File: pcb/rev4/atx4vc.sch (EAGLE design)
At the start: 48 parts, among them IC1 MY_7905DT, J2 ATX24RH

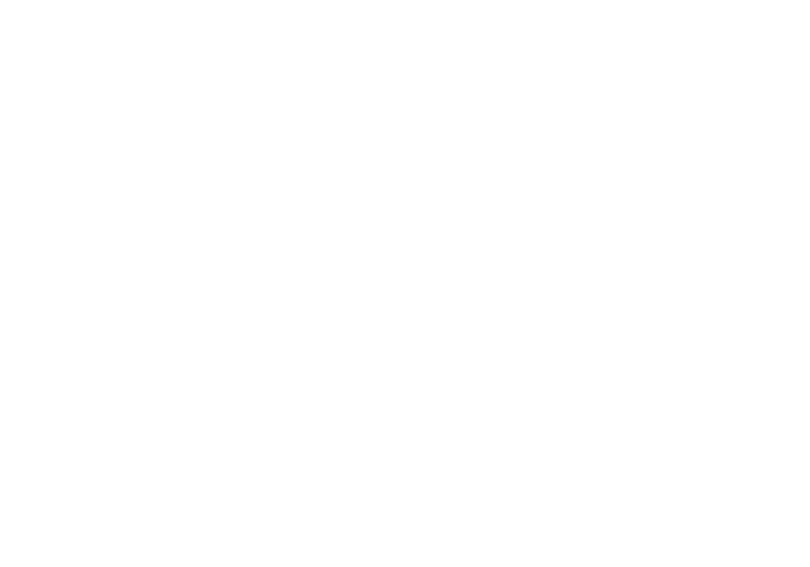
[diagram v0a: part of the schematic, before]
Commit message: trying out power ic
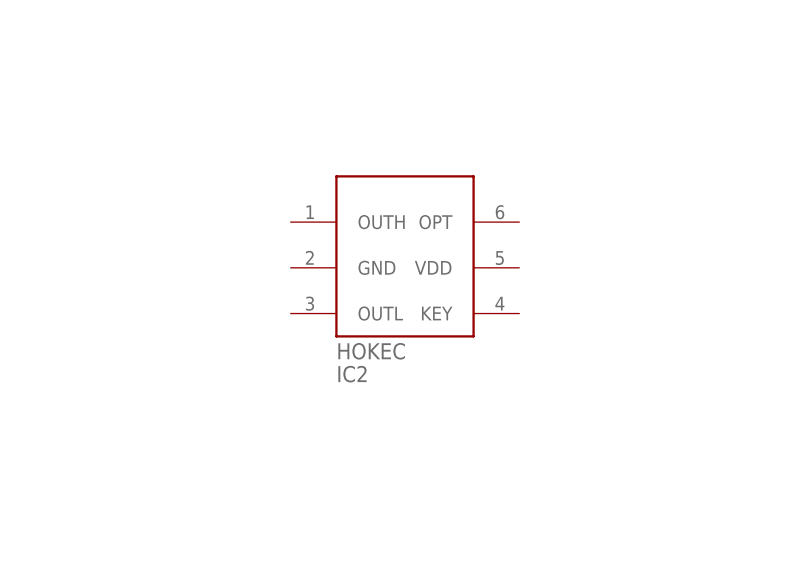
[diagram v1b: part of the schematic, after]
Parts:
- added IC2: MAX486X/SOT, pmm:MAX486X/SOT
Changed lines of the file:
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@@
 <layer number="154" name="FabDoc2" color="7" fill="1" visible="yes" active="yes"/>
 <layer number="155" name="FabDoc3" color="7" fill="1" visible="yes" active="yes"/>
+<layer number="156" name="gesam-Maß" color="7" fill="1" visible="yes" active="yes"/>
+<layer number="157" name="FaceMchng" color="7" fill="1" visible="yes" active="yes"/>
+<layer number="158" name="FaceMMeas" color="7" fill="1" visible="yes" active="yes"/>
+<layer number="159" name="Geh-Bear2" color="7" fill="1" visible="yes" active="yes"/>
+<layer number="160" name="O_Dim" color="7" fill="1" visible="yes" active="yes"/>
+<layer number="161" name="tomplace2" color="7" fill="1" visible="yes" active="yes"/>
 <layer number="166" name="AntennaArea" color="7" fill="1" visible="yes" active="yes"/>
 <layer number="168" name="4mmHeightArea" color="7" fill="1" visible="yes" active="yes"/>
@@
 <layer number="250" name="Descript" color="3" fill="1" visible="no" active="no"/>
 <layer number="251" name="SMDround" color="12" fill="11" visible="no" active="no"/>
+<layer number="252" name="BR-BS" color="7" fill="1" visible="yes" active="yes"/>
 <layer number="253" name="Extra" color="7" fill="1" visible="yes" active="yes"/>
 <layer number="254" name="cooling" color="7" fill="1" visible="yes" active="yes"/>
@@
 <part name="TP2" library="testpad" library_urn="urn:adsk.eagle:library:385" deviceset="TP" device="TP12R" package3d_urn="urn:adsk.eagle:package:27963/1"/>
 <part name="JP1" library="appleii" deviceset="4PIN_FAN" device=""/>
+<part name="IC2" library="pmm" deviceset="MAX486X" device="/SOT"/>
 </parts>
 <sheets>
@@
 </instance>
 <instance part="JP1" gate="A" x="223.52" y="-93.98" smashed="yes" rot="R180"/>
+<instance part="IC2" gate="G$1" x="121.92" y="81.28" smashed="yes">
+<attribute name="NAME" x="114.3" y="66.04" size="1.778" layer="95" font="vector"/>
+</instance>
 </instances>
 <busses>

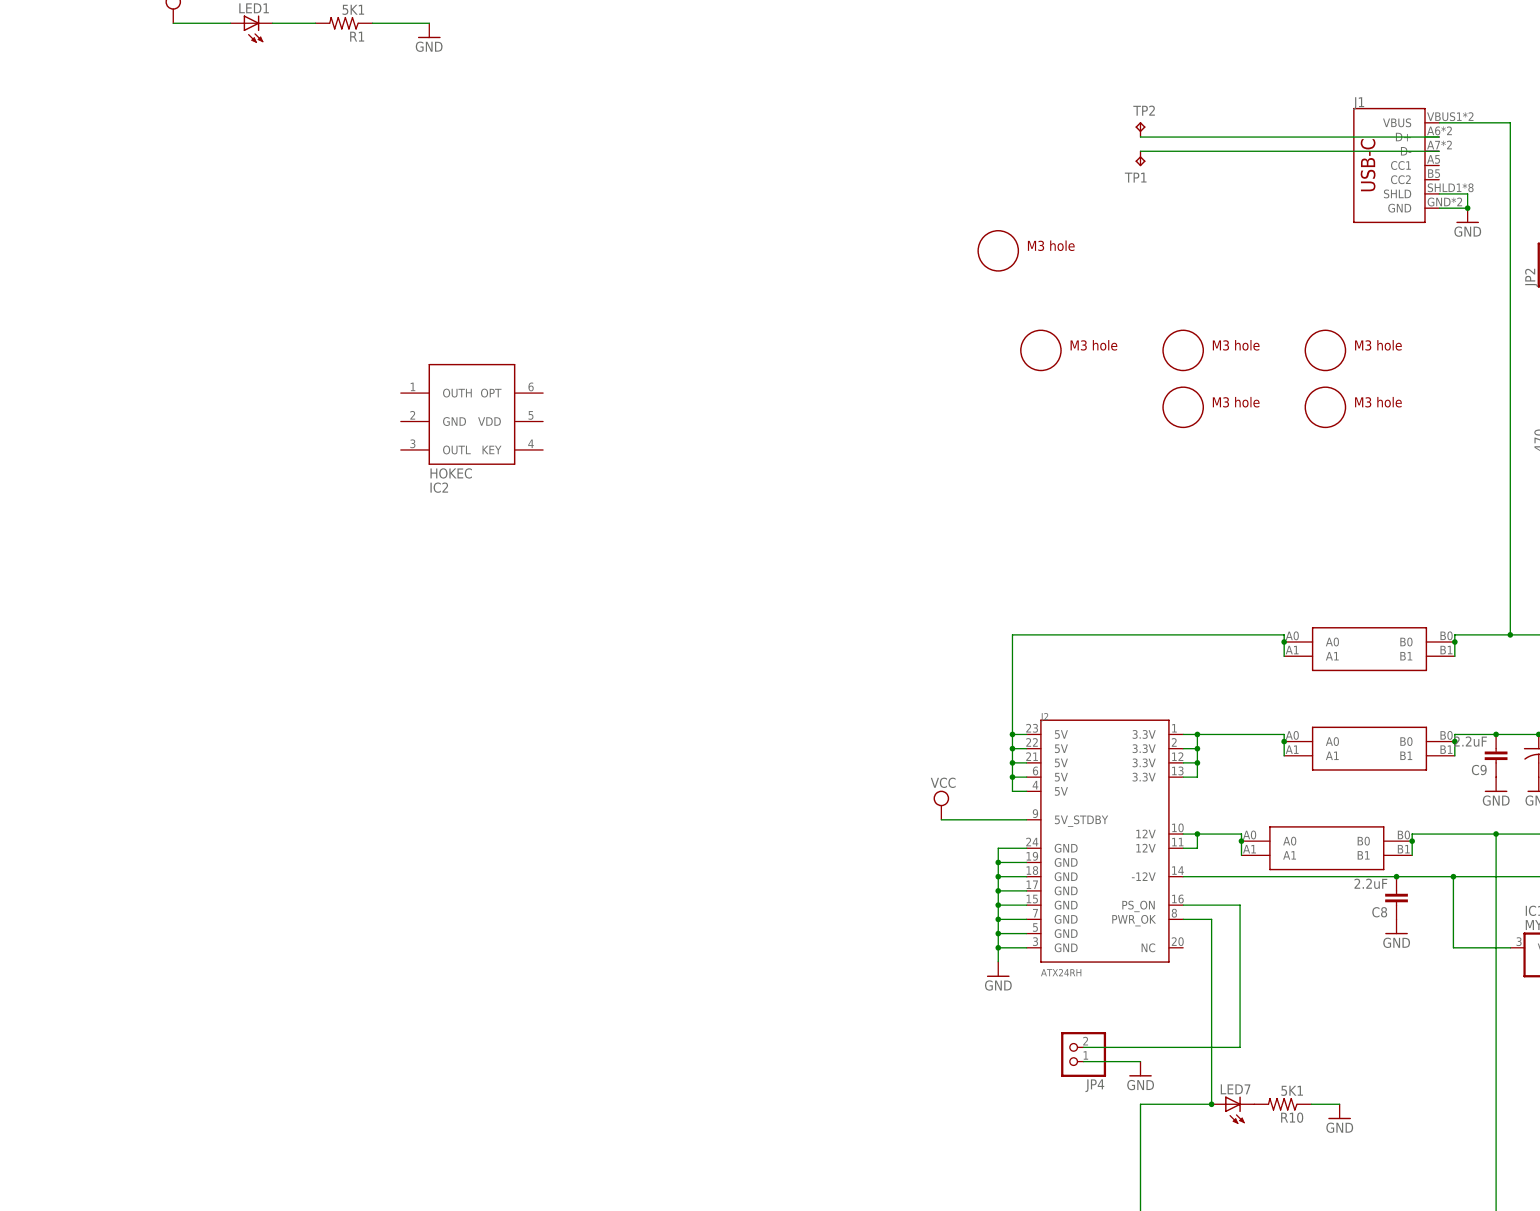
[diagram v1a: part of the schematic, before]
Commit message: trying out power ic
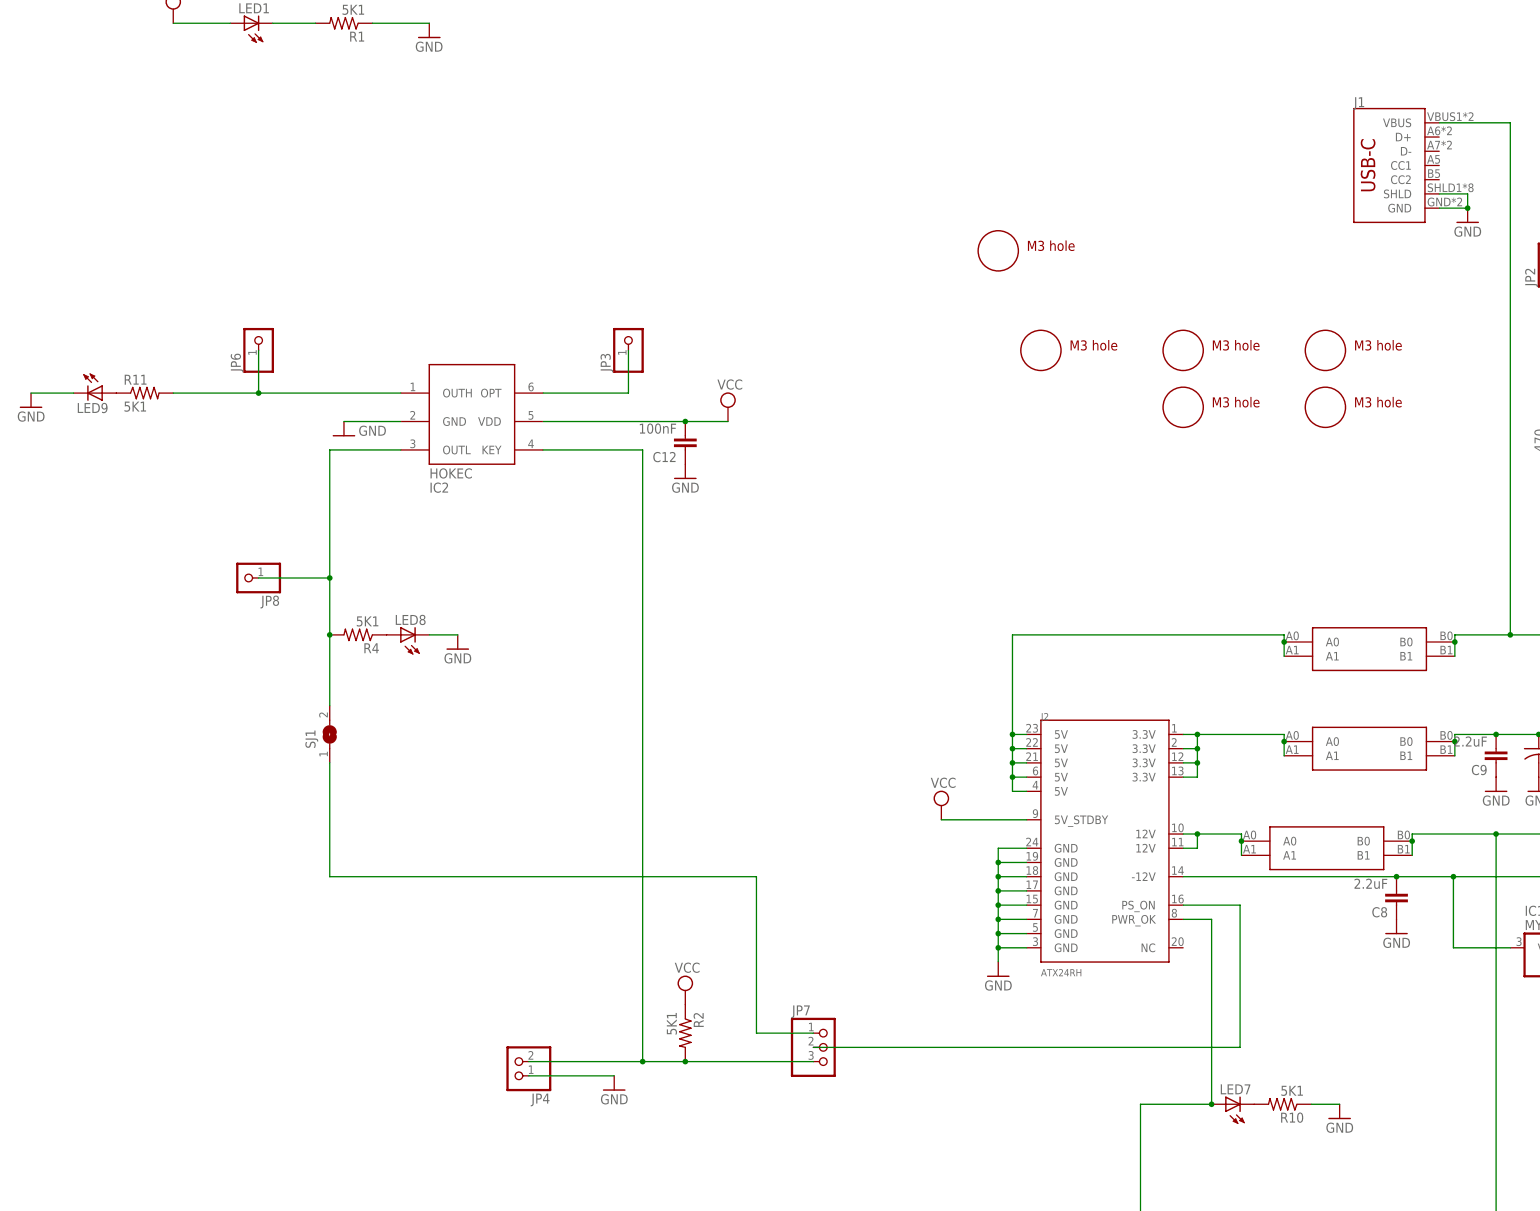
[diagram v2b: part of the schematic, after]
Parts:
- removed TP1, TP2: TPTP12R, testpad:TPTP12R
- added C12: 100nF, atx_power_control:CAP0805
- added JP3, JP6, JP8: (no value), adafruit_changed:PINHD-1X1CB
- added JP7: (no value), adafruit_changed:PINHD-1X3CB
- added LED8, LED9: (no value), adafruit:LEDCHIP-LED0805
- added R11, R2, R4: 5K1, atx_power_control:RESISTOR0805-RES
- added SJ1: (no value), jumper:SJ
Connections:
- removed net N$2: J1.D+, TP2.TP
- removed net N$4: J1.D-, TP1.TP
- new net N$12: IC2.KEY, JP4.2, JP7.3, R2.2
- new net N$13: LED8.A, R4.1
- new net N$16: LED9.A, R11.1
- new net N$19: IC2.OUTL, JP8.1, R4.2, SJ1.2
- new net N$3: IC2.OPT, JP3.1
- new net N$6: JP7.1, SJ1.1
- new net N$7: IC2.OUTH, JP6.1, R11.2
- net GND: now also C12.1, IC2.GND, LED8.C, LED9.C
- net N$15: now also JP7.2; no longer JP4.2
- net VCC: now also C12.2, IC2.VDD, R2.1
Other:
- moved on the sheet: JP4
